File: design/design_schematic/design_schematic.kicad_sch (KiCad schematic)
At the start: 145 parts, among them IC1 XC9291B33D0R-G, IC2 XC9148G50CER-G, IC4 74AHCT125PW,118, J1 USB_C_Receptacle_USB2.0_16P, J2 Battery Pos, J3 Battery Neg, J4 OLED_128x32, J5 0781271220, J6 Conn_01x05, SW1 SW_SPST, SW2 SW_Push, U1 nRF52840, U2 BQ24072RGT, U3 USB6B1, U4 BQ27441-G1, U5 PEC11L-4015F-S0015, U6 PEC11L-4015F-S0015, X1 32MHz

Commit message: vbus routing
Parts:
- removed C37, C40, C43, C49: 100nF, ScottoKeebs_Components:Capacitor_0402, symbol Device:C_Small
- removed C46: 10uF, ScottoKeebs_Components:Capacitor_0402, symbol Device:C_Small
- removed J6: Conn_01x05, symbol Connector_Generic:Conn_01x05
- removed L3: 10uH, Inductor_SMD:L_0402_1005Metric, symbol Device:L_Small
- removed L4: 10uH, Inductor_SMD:L_0201_0603Metric, symbol Device:L_Small
- removed R13: 10k, symbol Device:R
- removed SW1: SW_SPST, symbol Switch:SW_SPST
- removed SW2: SW_Push, symbol Switch:SW_Push
- removed U1: nRF52840, Package_DFN_QFN:Nordic_AQFN-73-1EP_7x7mm_P0.5mm, symbol MCU_Nordic:nRF52840
- added C29, C30, C32, C33: 100nF, ScottoKeebs_Components:Capacitor_0603, symbol Device:C_Small
- added C35: 22uF, ScottoKeebs_Components:Capacitor_0603, symbol Device:C_Small
- added IC3: nRF52833-QDAA-R7, SamacSys_Parts:QFN40P500X500X90-41N-D, symbol SamacSys_Parts:nRF52833-QDAA-R7
- added IC5: MCP23018T-E_SS, SamacSys_Parts:SOP65P780X200-24N, symbol SamacSys_Parts:MCP23018T-E_SS
- added IC6: XC9291B33D1R-G, XC9290A07E1RG, symbol SamacSys_Parts:XC9291B33D1R-G
- added J6: Conn_01x04, symbol Connector_Generic:Conn_01x04
- added S26: CL-SA-12C4-22, SamacSys_Parts:CLSA12C422, symbol SamacSys_Parts:CL-SA-12C4-22
- C1, C2: value 12pF -> 4.7uF; footprint ScottoKeebs_Components:Capacitor_0402 -> ScottoKeebs_Components:Capacitor_0603
- C10, C13, C17, C18, C22, C23, C24, C25, C26, C27, C28, C31, C7, C8, C9: footprint ScottoKeebs_Components:Capacitor_0402 -> ScottoKeebs_Components:Capacitor_0603
- C11: value 100pF -> 820pF; footprint ScottoKeebs_Components:Capacitor_0402 -> ScottoKeebs_Components:Capacitor_0603
- C12: value 100nF -> 100pF; footprint ScottoKeebs_Components:Capacitor_0402 -> ScottoKeebs_Components:Capacitor_0603
- C14: value 1uF -> 12pF
- C15: value 1uF -> 1.2pF
- C16: value 47nF -> 1pF; footprint ScottoKeebs_Components:Capacitor_0402 -> ScottoKeebs_Components:Capacitor_0603
- C19: value 4.7uF -> 12pF
- C20, C21: value 4.7uF -> 100nF
- C3: value 0.8pF -> 100nF; footprint ScottoKeebs_Components:Capacitor_0402 -> ScottoKeebs_Components:Capacitor_0603
- C34: value 100nF -> 10uF; footprint ScottoKeebs_Components:Capacitor_0402 -> ScottoKeebs_Components:Capacitor_0603
- C4: value 0.5pF -> 4.7uF; footprint ScottoKeebs_Components:Capacitor_0402 -> ScottoKeebs_Components:Capacitor_0603
- C5: value 100nF -> 1uF; footprint ScottoKeebs_Components:Capacitor_0402 -> ScottoKeebs_Components:Capacitor_0603
- C6: value 4.7uF -> 1uF
- F1: footprint (none) -> SamacSys_Parts:0603L050SLYR
- IC2: footprint (none) -> SamacSys_Parts:XC9147_8_USP-6C
- J2, J3: footprint (none) -> Connector_Wire:SolderWire-2.5sqmm_1x01_D2.4mm_OD3.6mm
- L1: footprint Inductor_SMD:L_0402_1005Metric -> Inductor_SMD:L_0603_1608Metric
- L2: value 15nH -> 2.2nH; footprint Inductor_SMD:L_0201_0603Metric -> Inductor_SMD:L_0603_1608Metric
- L5, L6: footprint (none) -> Inductor_SMD:L_0603_1608Metric
- R1, R10, R11, R12, R2, R3, R4, R5, R6, R7, R8, R9: footprint (none) -> Resistor_SMD:R_0603_1608Metric
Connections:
- net VDD_HV is gone; now on net GND: C19.2
- net 2A: now also IC3.23 (P0.10)
- net 3V3: now also C1.2, C20.2, C5.1, C7.1, C8.1, IC3.18 (VDD_2), IC3.30 (VDD_3), IC3.40 (VDD_4), IC3.8 (VDD_1), IC3.9 (VDDH), IC5.10 (VDD), J6.1 (Pin_1); no longer C12.2, C14.2, C6.2, C7.2, C8.2
- net 5V: now also C21.1, C29.1, C30.1, C32.1, C33.1
- net CCW: now also IC3.15 (P0.17)
- net CCW2: now also IC3.16 (P0.18)
- net CHG: now also IC5.19 (GPA2)
- net CW: now also IC3.14 (P0.15)
- net CW2: now also IC3.17 (P0.20)
- net Column 0: now also IC3.36 (P0.31)
- net Column 1: now also IC3.35 (P0.30)
- net Column 2: now also IC3.34 (P0.29)
- net Column 3: now also IC3.33 (P0.28)
- net Column 4: now also IC3.32 (P0.02)
- net Column 5: now also IC3.31 (P0.03)
- net D+: now also IC3.13 (D+)
- net D-: now also IC3.12 (D-)
- net GND: now also C11.2, C12.2, C14.2, C16.1, C2.1, C21.2, C3.1, C5.2, C7.2, C8.2, C29.2, C30.2, C32.2, C33.2, C35.2, IC3.25 (VSS_PA), IC3.37 (VSS_1), IC3.41 (VSS_2), IC5.1 (VSS), J6.2 (Pin_2); no longer C11.1, C12.1, C14.1, C16.2, C19.1, C2.2, C21.1, C3.2, C5.1, C7.1, C8.1
- net NO: now also IC5.17 (GPA0)
- net NO2: now also IC5.18 (GPA1)
- net Row 0: now also IC3.4 (P0.04)
- net Row 1: now also IC3.5 (P0.05)
- net Row 2: now also IC3.6 (P1.09)
- net Row 3: now also IC3.7 (P0.11)
- net SCL: now also R10.1, IC3.2 (P0.00), IC5.11 (SCL); no longer R11.1
- net SDA: now also R11.1, IC3.3 (P0.01), IC5.12 (SDA); no longer R10.1
- net VBUS: now also C2.2, C23.2, F1.2, U2.13 (IN), U2.6 (EN1), U3.1 (VBUS), U3.8 (VBUS), C35.1, IC3.10 (VBUS); no longer C21.2
- net at L2.2: now also C15.1, L1.2
- net at X1.1: now also C14.1, IC3.29 (XC2); no longer C2.1
- net at X1.2: now also C19.1, IC3.28 (XC1); no longer C1.2
- net at D11.4 (DIN): now also D15.2 (DOUT); no longer D10.2 (DOUT)
- net at D10.4 (DIN): now also D6.2 (DOUT); no longer D9.2 (DOUT)
- net at D13.2 (DOUT): now also D17.4 (DIN); no longer D14.4 (DIN)
- net at D13.4 (DIN): now also D9.2 (DOUT); no longer D12.2 (DOUT)
- net at D24.4 (DIN): now also D22.2 (DOUT); no longer D23.2 (DOUT)
- net at D23.4 (DIN): now also D21.2 (DOUT); no longer D22.2 (DOUT)
- net at C10.1, C25.1, IC1.1 (EN)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: now also S26.1 (COM)
- net at D8.2 (DOUT): now also D4.4 (DIN); no longer D9.4 (DIN)
- net at D7.2 (DOUT): now also D3.4 (DIN); no longer D8.4 (DIN)
- net at D7.4 (DIN): now also D11.2 (DOUT); no longer D6.2 (DOUT)
- net at L1.1: now also C16.2, IC3.24 (ANT); no longer C4.2
- net at D22.4 (DIN): now also D18.2 (DOUT); no longer D21.2 (DOUT)
- net at D21.4 (DIN): now also D17.2 (DOUT); no longer D20.2 (DOUT)
- net at D16.4 (DIN): now also D20.2 (DOUT); no longer D15.2 (DOUT)
- net at D15.4 (DIN): now also D19.2 (DOUT); no longer D14.2 (DOUT)
- net at D16.2 (DOUT): now also D12.4 (DIN); no longer D17.4 (DIN)
- net at D19.4 (DIN): now also D23.2 (DOUT); no longer D18.2 (DOUT)
- net at D18.4 (DIN): now also D14.2 (DOUT); no longer D17.2 (DOUT)
- net at D2.4 (DIN): now also D3.2 (DOUT); no longer D1.2 (DOUT)
- net at D20.4 (DIN): now also D24.2 (DOUT); no longer D19.2 (DOUT)
- net at D2.2 (DOUT): now also D6.4 (DIN); no longer D3.4 (DIN)
- net at U2.10 (OUT), U2.11 (OUT): now also S26.2 (NO)
- net at D5.2 (DOUT): now also D9.4 (DIN); no longer D6.4 (DIN)
- net at D5.4 (DIN): now also D1.2 (DOUT); no longer D4.2 (DOUT)
- new net: C3.2, IC3.1 (DEC1)
- new net: C11.1, IC3.21 (DEC5)
- new net: D12.2 (DOUT), D8.4 (DIN)
- new net: C4.2, IC3.11 (DECUSB)
- new net: IC3.19 (SWDIO), J6.4 (Pin_4)
- new net: IC3.20 (SWDCLK), J6.3 (Pin_3)
- new net: C12.1, IC3.27 (DEC3)
- new net: D10.2 (DOUT), D14.4 (DIN)
- new net DEC4: C6.2, IC3.26 (DEC6), IC3.38 (DEC4)
- new net INTA: IC3.22 (P0.09), IC5.16 (INTA)
- new net RF: L2.1
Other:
- note added: "GPIO Expander"
- note added: "nRF52833 Module"
- note removed: "nRF52840 Module"
- moved on the sheet: C25

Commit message: prepare to change switch footprint
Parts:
- removed IC1: XC9291B33D0R-G, SamacSys_Parts:XC9290A07E0RG, symbol SamacSys_Parts:XC9291B33D0R-G
- removed L5: 1uH, Inductor_SMD:L_0603_1608Metric, symbol Device:L
- added L3: 1uH, Inductor_SMD:L_0603_1608Metric, symbol Device:L
- IC6: footprint XC9290A07E1RG -> SamacSys_Parts:XC9290A07E1RG
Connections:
- net 3V3: now also IC6.1 (VOUT), L3.1
- net GND: now also IC6.6 (GND)
- net at C10.1, C25.1, IC2.1 (BAT)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: now also IC6.3 (EN), IC6.4 (VIN)
- net at IC6.5 (LX): now also L3.2
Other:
- moved on the sheet: IC6

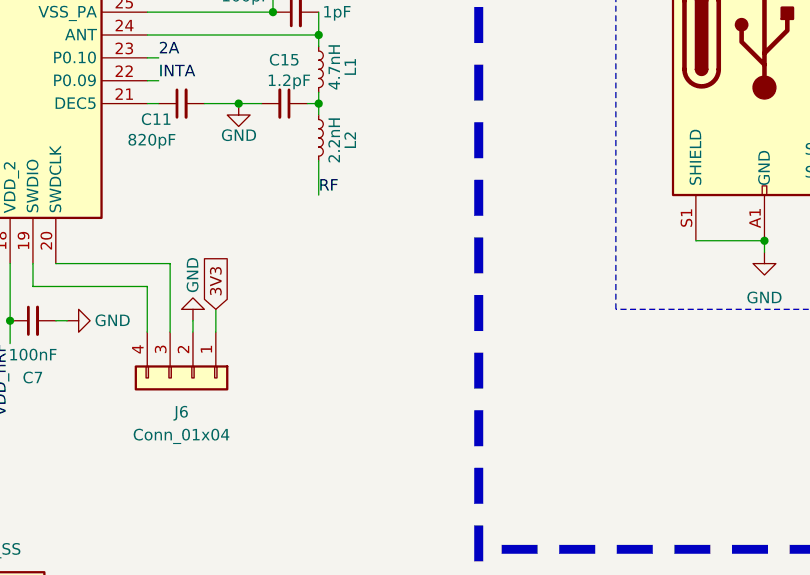
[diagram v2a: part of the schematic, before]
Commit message: prepare to reroute for antenna
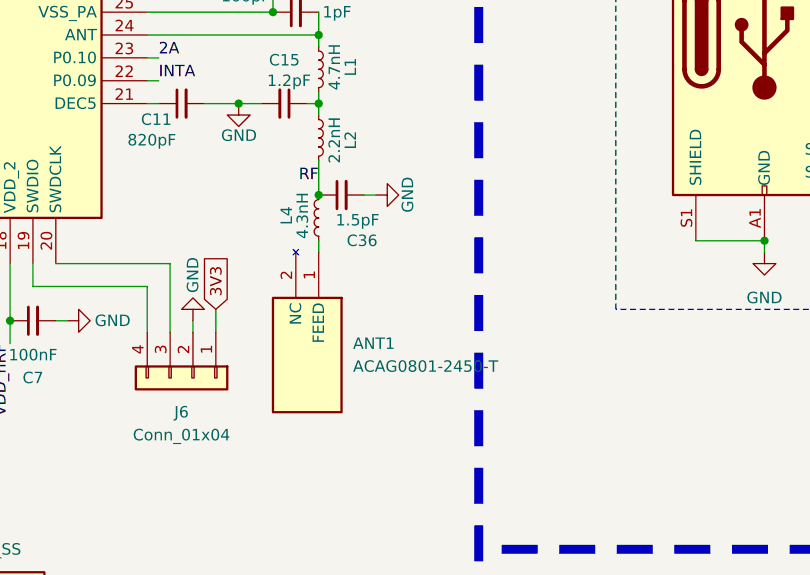
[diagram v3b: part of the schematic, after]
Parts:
- added ANT1: ACAG0801-2450-T, ANTC8010X110N, symbol SamacSys_Parts:ACAG0801-2450-T
- added C36: 1.5pF, ScottoKeebs_Components:Capacitor_0603, symbol Device:C_Small
- added L4: 4.3nH, Inductor_SMD:L_0603_1608Metric, symbol Device:L_Small
- S1, S10, S11, S12, S13, S14, S15, S16, S17, S18, S19, S2, S20, S21, S22, S23, S24, S3, S4, S5, S6, S7, S8, S9: footprint ScottoKeebs_Hotswap:Hotswap_Choc_V1_1.00u -> ScottoKeebs_Hotswap:Hotswap_Choc_V1V2_Plated_1.00u
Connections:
- net GND: now also C36.2
- net RF: now also C36.1, L4.1
- new net: ANT1.1 (FEED), L4.2

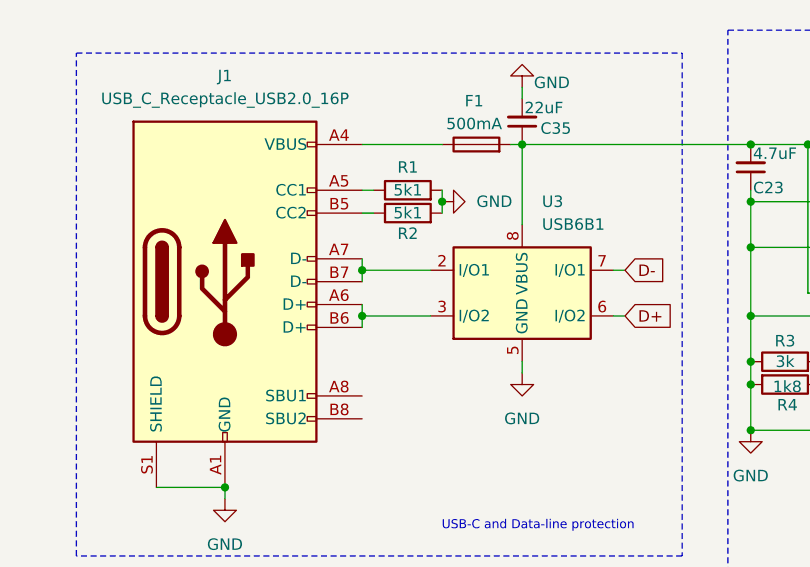
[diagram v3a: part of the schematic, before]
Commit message: begin to relocate usb c data lines
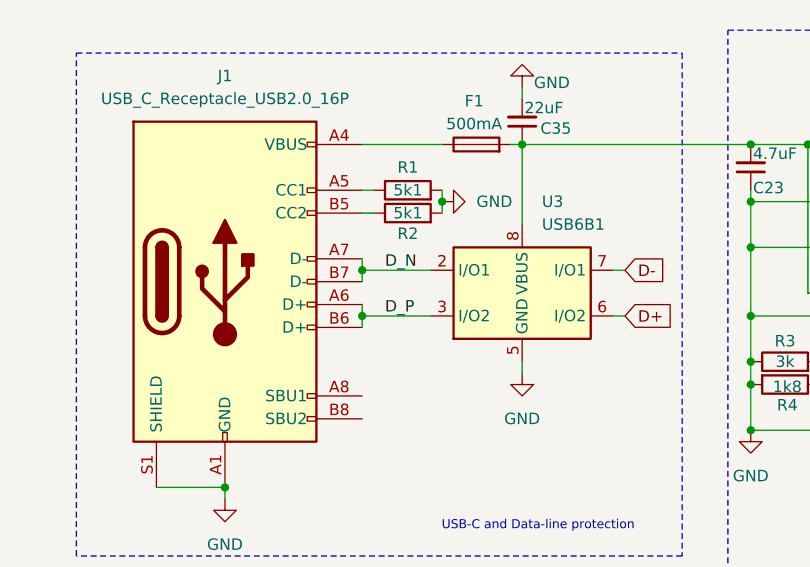
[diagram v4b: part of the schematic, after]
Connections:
- net D_N: now reaches J1.A7 (D-), J1.B7 (D-), U3.2 (I/O1)
- net D_P: now reaches J1.A6 (D+), J1.B6 (D+), U3.3 (I/O2)
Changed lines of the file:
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@@
+		)
+	)
+	(label "D_N"
+		(at 177.8 105.41 0)
+		(fields_autoplaced yes)
+		(effects
+			(font
+				(size 1.27 1.27)
+			)
+			(justify left bottom)
 		)
 	)
@@
 		)
 	)
+	(label "D_P"
+		(at 177.8 110.49 0)
+		(fields_autoplaced yes)
+		(effects
+			(font
+				(size 1.27 1.27)
+			)
+			(justify left bottom)
+		)
+	)

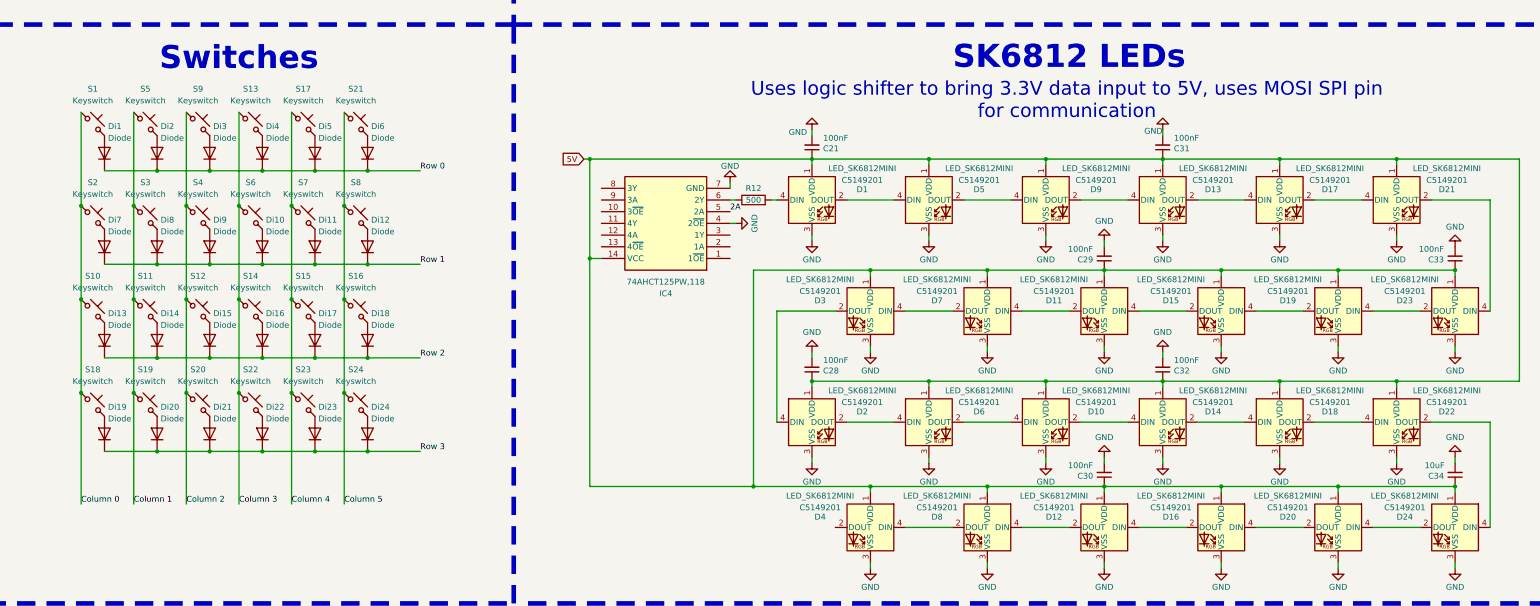
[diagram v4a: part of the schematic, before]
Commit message: finish switch routing
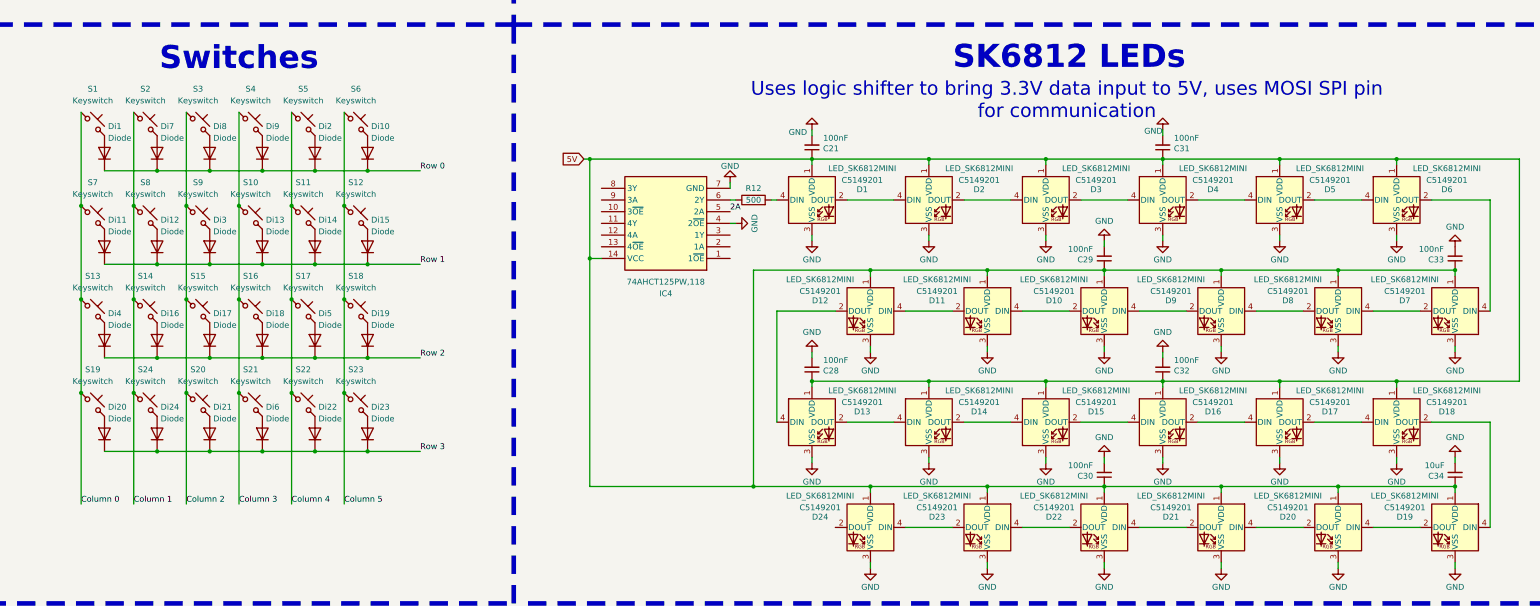
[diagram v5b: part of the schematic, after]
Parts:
- ANT1: footprint ANTC8010X110N -> SamacSys_Parts:ANTC8010X110N
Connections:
- net Column 0: now also S13.1, S19.1, S7.1; no longer S10.1, S18.1, S2.1
- net Column 1: now also S14.1, S2.1, S24.1, S8.1; no longer S11.1, S19.1, S3.1, S5.1
- net Column 2: now also S15.1, S3.1; no longer S12.1, S4.1
- net Column 3: now also S10.1, S16.1, S21.1, S4.1; no longer S13.1, S14.1, S22.1, S6.1
- net Column 4: now also S11.1, S22.1, S5.1; no longer S15.1, S23.1, S7.1
- net Column 5: now also S12.1, S18.1, S23.1, S6.1; no longer S16.1, S21.1, S24.1, S8.1
- net Row 0: now also Di10.1 (K), Di7.1 (K), Di8.1 (K), Di9.1 (K); no longer Di3.1 (K), Di4.1 (K), Di5.1 (K), Di6.1 (K)
- net Row 1: now also Di13.1 (K), Di14.1 (K), Di15.1 (K), Di3.1 (K); no longer Di10.1 (K), Di7.1 (K), Di8.1 (K), Di9.1 (K)
- net Row 2: now also Di19.1 (K), Di4.1 (K), Di5.1 (K); no longer Di13.1 (K), Di14.1 (K), Di15.1 (K)
- net Row 3: now also Di6.1 (K); no longer Di19.1 (K)
- net at D6.2 (DOUT): now also D7.4 (DIN); no longer D10.4 (DIN)
- net at D6.4 (DIN): now also D5.2 (DOUT); no longer D2.2 (DOUT)
- net at D17.2 (DOUT): now also D18.4 (DIN); no longer D21.4 (DIN)
- net at D17.4 (DIN): now also D16.2 (DOUT); no longer D13.2 (DOUT)
- net at D3.2 (DOUT): now also D4.4 (DIN); no longer D2.4 (DIN)
- net at D3.4 (DIN): now also D2.2 (DOUT); no longer D7.2 (DOUT)
- net at D15.2 (DOUT): now also D16.4 (DIN); no longer D11.4 (DIN)
- net at D15.4 (DIN): now also D14.2 (DOUT); no longer D19.2 (DOUT)
- net at D12.4 (DIN): now also D11.2 (DOUT); no longer D16.2 (DOUT)
- net at D20.2 (DOUT): now also D21.4 (DIN); no longer D16.4 (DIN)
- net at D21.2 (DOUT): now also D22.4 (DIN); no longer D23.4 (DIN)
- net at D20.4 (DIN): now also D19.2 (DOUT); no longer D24.2 (DOUT)
- net at D24.4 (DIN): now also D23.2 (DOUT); no longer D22.2 (DOUT)
- net at D13.4 (DIN): now also D12.2 (DOUT); no longer D9.2 (DOUT)
- net at D18.2 (DOUT): now also D19.4 (DIN); no longer D22.4 (DIN)
- net at D1.2 (DOUT): now also D2.4 (DIN); no longer D5.4 (DIN)
- net at D8.2 (DOUT): now also D9.4 (DIN); no longer D4.4 (DIN)
- net at D8.4 (DIN): now also D7.2 (DOUT); no longer D12.2 (DOUT)
- net at D14.4 (DIN): now also D13.2 (DOUT); no longer D10.2 (DOUT)
- net at D4.2 (DOUT): now also D5.4 (DIN)
- new net: D22.2 (DOUT), D23.4 (DIN)
- new net: D10.2 (DOUT), D11.4 (DIN)
- new net: D10.4 (DIN), D9.2 (DOUT)
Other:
- moved on the sheet: D10, D11, D12, D13, D14, D15, D16, D17, D18, D19, D2, D21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

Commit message: no errors drc
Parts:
- added 3V3_2, 3v3_1, 5V_1, 5V_2, 5V_3, BAT_1, GND1, GND2, GND3, GND4, VBUS_1, VBUS_USB1: TestPoint, TestPoint:TestPoint_Pad_D1.5mm, symbol Connector:TestPoint
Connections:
- net 3V3: now also 3V3_2.1, 3v3_1.1
- net 5V: now also 5V_1.1, 5V_2.1, 5V_3.1
- net GND: now also GND1.1, GND2.1, GND3.1, GND4.1
- net VBUS: now also VBUS_1.1
- net BAT: now reaches C17.1, C18.1, J2.1 (Pin_1), U2.2 (BAT), U2.3 (BAT), U4.6 (BAT)
- net BAT: now also BAT_1.1
- net at D20.4 (DIN): now also D24.2 (DOUT); no longer D19.2 (DOUT)
- net at D24.4 (DIN): now also D19.2 (DOUT); no longer D23.2 (DOUT)
- net OUT: now reaches S26.2 (NO), U2.10 (OUT), U2.11 (OUT)
- net VBUS_USB: now reaches F1.1, J1.A4 (VBUS), J1.A9 (VBUS), J1.B4 (VBUS), J1.B9 (VBUS)
- net VBUS_USB: now also VBUS_USB1.1
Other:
- moved on the sheet: C24, C9, D20, D21, D22, D23, D24, J4, J5, U5, U6

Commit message: routed no errors
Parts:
- removed C24: 100nF, ScottoKeebs_Components:Capacitor_0603, symbol Device:C_Small
- removed J5: 0781271220, SamacSys_Parts:0781271220, symbol SamacSys_Parts:0781271220
- added 5V_4: TestPoint, TestPoint:TestPoint_Pad_D1.5mm, symbol Connector:TestPoint
- added C37: 100nF, ScottoKeebs_Components:Capacitor_0603, symbol Device:C_Small
- added J5: SFV12R-1STBE1HLF, SFV12R1STBE1HLF, symbol SamacSys_Parts:SFV12R-1STBE1HLF
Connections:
- net 3V3: now also C37.1, J5.12
- net GND: now also C37.2, J5.11
- net OUT: now also 5V_4.1
- net SCL: now also J5.9
- net SDA: now also J5.10
- new net: J5.MP1, J5.MP2, J5.MP3
- new net: J5.MP4, J5.MP5, J5.MP6
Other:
- moved on the sheet: 5V_3, BAT_1

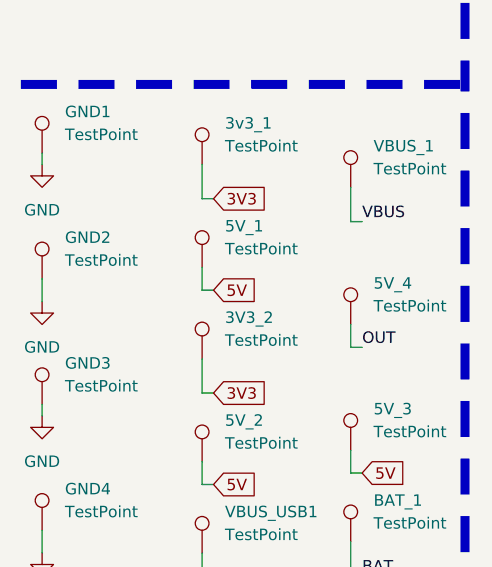
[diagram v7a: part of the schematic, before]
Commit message: begin to remove unnecessary vias
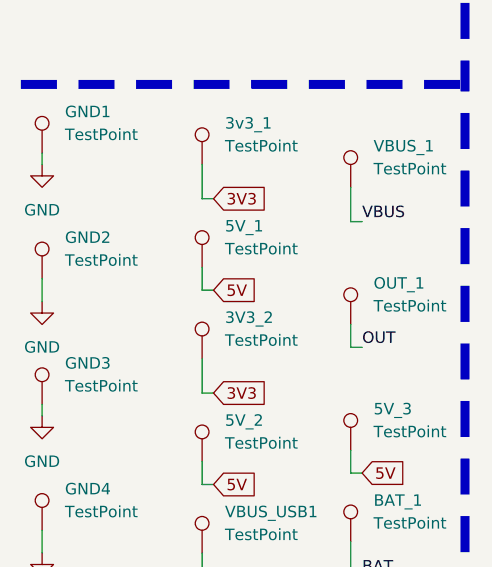
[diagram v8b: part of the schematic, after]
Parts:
- renumbered 5V_4 to OUT_1
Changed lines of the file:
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@@
 		(dnp no)
 		(fields_autoplaced yes)
-		(property "Reference" "5V_4"
+		(property "Reference" "OUT_1"
 			(at 355.6 185.9279 0)
 			(effects
@@
 			(project "design_schematic"
 				(path "/0454547d-f090-46a4-b0ab-f58aec48f156"
-					(reference "5V_4")
+					(reference "OUT_1")
 					(unit 1)
 				)
